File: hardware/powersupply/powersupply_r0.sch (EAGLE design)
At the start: 4 parts

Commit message: basic placement
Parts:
- added C1, C2: (no value), SparkFun-Passives:CAP_POLPTH4
- added C3, C4, C5, C6: (no value), SparkFun-Passives:CAP_POLPTH1
- added F1, F2, F3, F4, F5: FUSEX20MM, SparkFun-Passives:FUSEX20MM
- added U$1, U$2, U$3, U$4, U$5: SCREWTERMINAL-2PIN, openct:SCREWTERMINAL-2PIN
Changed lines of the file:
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@@
 <part name="IC3" library="SparkFun-PowerIC" deviceset="V_REG_78XX" device="SINK"/>
 <part name="IC4" library="SparkFun-PowerIC" deviceset="V_REG_78XX" device="SINK"/>
+<part name="U$1" library="openct" deviceset="SCREWTERMINAL-2PIN" device=""/>
+<part name="U$2" library="openct" deviceset="SCREWTERMINAL-2PIN" device=""/>
+<part name="U$3" library="openct" deviceset="SCREWTERMINAL-2PIN" device=""/>
+<part name="U$4" library="openct" deviceset="SCREWTERMINAL-2PIN" device=""/>
+<part name="U$5" library="openct" deviceset="SCREWTERMINAL-2PIN" device=""/>
+<part name="F1" library="SparkFun-Passives" deviceset="FUSE" device="X20MM"/>
+<part name="F2" library="SparkFun-Passives" deviceset="FUSE" device="X20MM"/>
+<part name="F3" library="SparkFun-Passives" deviceset="FUSE" device="X20MM"/>
+<part name="F4" library="SparkFun-Passives" deviceset="FUSE" device="X20MM"/>
+<part name="C1" library="SparkFun-Passives" deviceset="CAP_POL" device="PTH4"/>
+<part name="C2" library="SparkFun-Passives" deviceset="CAP_POL" device="PTH4"/>
+<part name="F5" library="SparkFun-Passives" deviceset="FUSE" device="X20MM"/>
+<part name="C3" library="SparkFun-Passives" deviceset="CAP_POL" device="PTH1"/>
+<part name="C4" library="SparkFun-Passives" deviceset="CAP_POL" device="PTH1"/>
+<part name="C5" library="SparkFun-Passives" deviceset="CAP_POL" device="PTH1"/>
+<part name="C6" library="SparkFun-Passives" deviceset="CAP_POL" device="PTH1"/>
 </parts>
 <sheets>
@@
 <instance part="IC3" gate="G$1" x="35.56" y="-40.64"/>
 <instance part="IC4" gate="G$1" x="35.56" y="-68.58"/>
+<instance part="U$1" gate="G$1" x="81.28" y="10.16"/>
+<instance part="U$2" gate="G$1" x="81.28" y="-15.24"/>
+<instance part="U$3" gate="G$1" x="81.28" y="-43.18"/>
+<instance part="U$4" gate="G$1" x="81.28" y="-71.12"/>
+<instance part="U$5" gate="G$1" x="-38.1" y="10.16"/>
+<instance part="F1" gate="G$1" x="55.88" y="12.7"/>
+<instance part="F2" gate="G$1" x="55.88" y="-12.7"/>
+<instance part="F3" gate="G$1" x="55.88" y="-40.64"/>
+<instance part="F4" gate="G$1" x="55.88" y="-68.58"/>
+<instance part="C1" gate="G$1" x="-48.26" y="-5.08"/>
+<instance part="C2" gate="G$1" x="-38.1" y="-5.08"/>
+<instance part="F5" gate="G$1" x="-66.04" y="2.54"/>
+<instance part="C3" gate="G$1" x="96.52" y="10.16"/>
+<instance part="C4" gate="G$1" x="96.52" y="-12.7"/>
+<instance part="C5" gate="G$1" x="96.52" y="-40.64"/>
+<instance part="C6" gate="G$1" x="96.52" y="-71.12"/>
 </instances>
 <busses>

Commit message: component layout complete
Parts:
- removed U$2, U$3, U$4: SCREWTERMINAL-2PIN, openct:SCREWTERMINAL-2PIN
- added C7: (no value), SparkFun-Passives:CAP_POLPTH1
- added CN17: 22-23-2041, con-molex:22-23-2041
- added JP1, JP3: M02JST-PTH-VERT, SparkFun-Connectors:M02JST-PTH-VERT
- added U$6: CON-USB, openct:CON-USB
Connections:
- new net GND: C3.-, C4.-, C5.-, C6.-, C7.-, CN17-2.S, CN17-3.S, IC1.GND, IC2.GND, IC3.GND, IC4.GND, U$1.2
- new net N$1: C3.+, F1.1, IC1.OUT
- new net N$2: C4.+, F2.1, IC2.OUT
- new net N$3: C5.+, F3.1, IC3.OUT
- new net N$4: C6.+, F4.1, IC4.OUT
- new net N$5: CN17-4.S, F4.2
- new net VBIAS: C7.+, CN17-1.S, U$1.1
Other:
- note added: "ARRAY POWER CONNECTOR"
- moved on the sheet: C3, C4, C5, C6, F1, F2, F3, F4

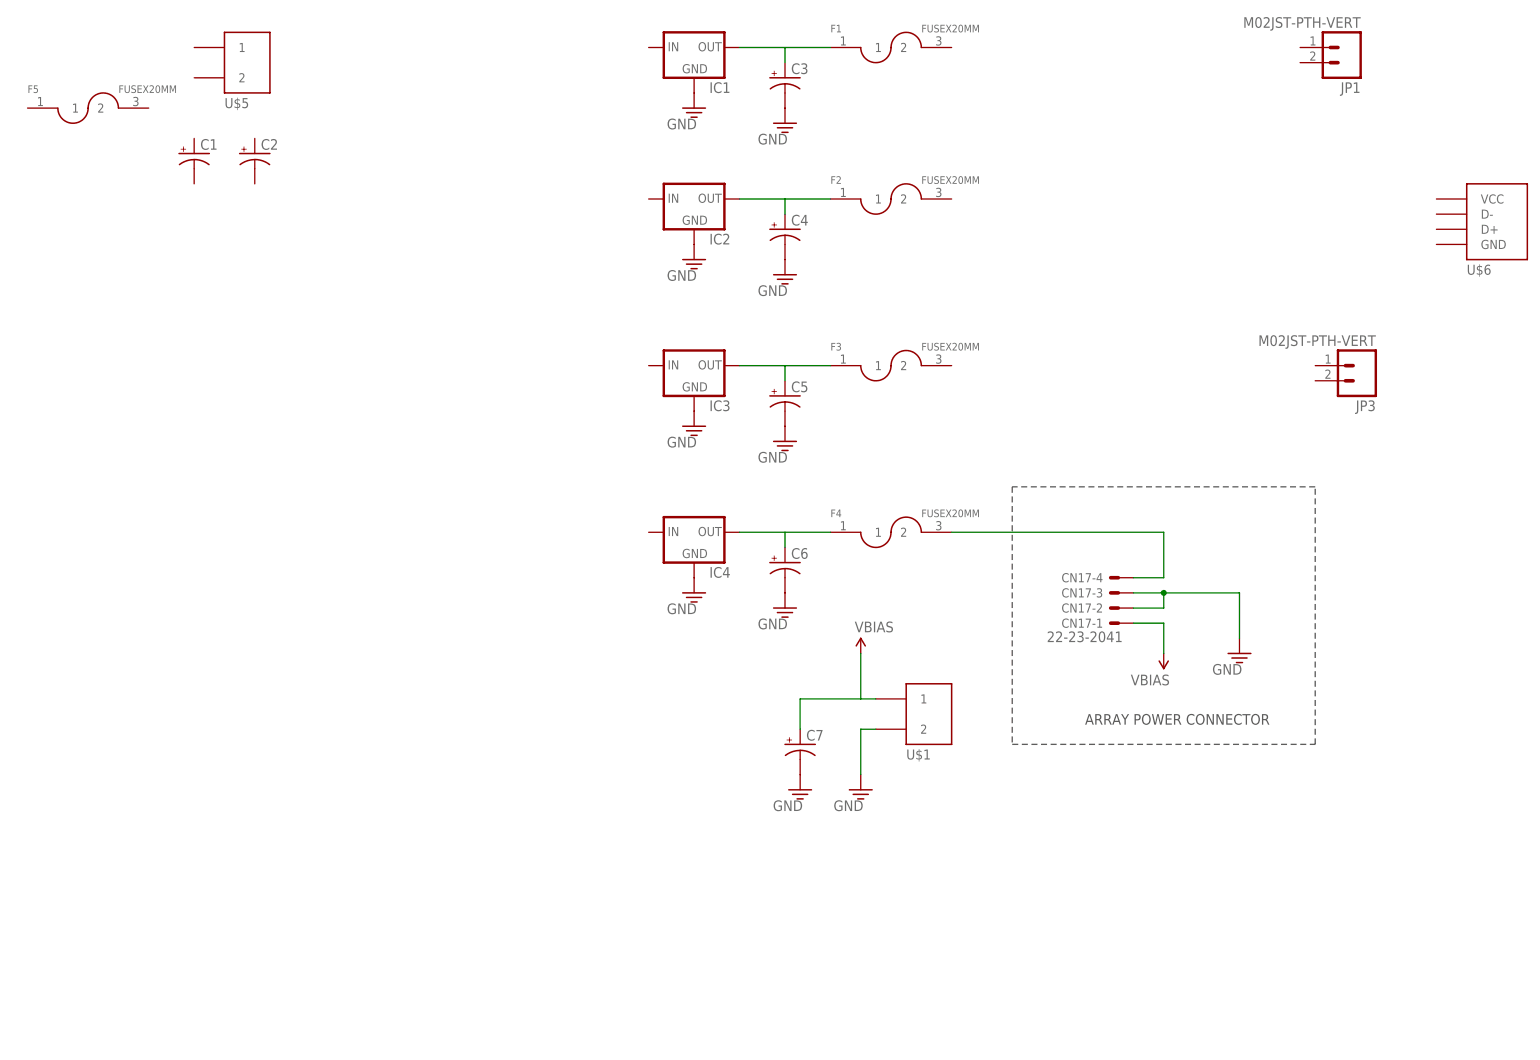
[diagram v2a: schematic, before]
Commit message: major routing on power supply board
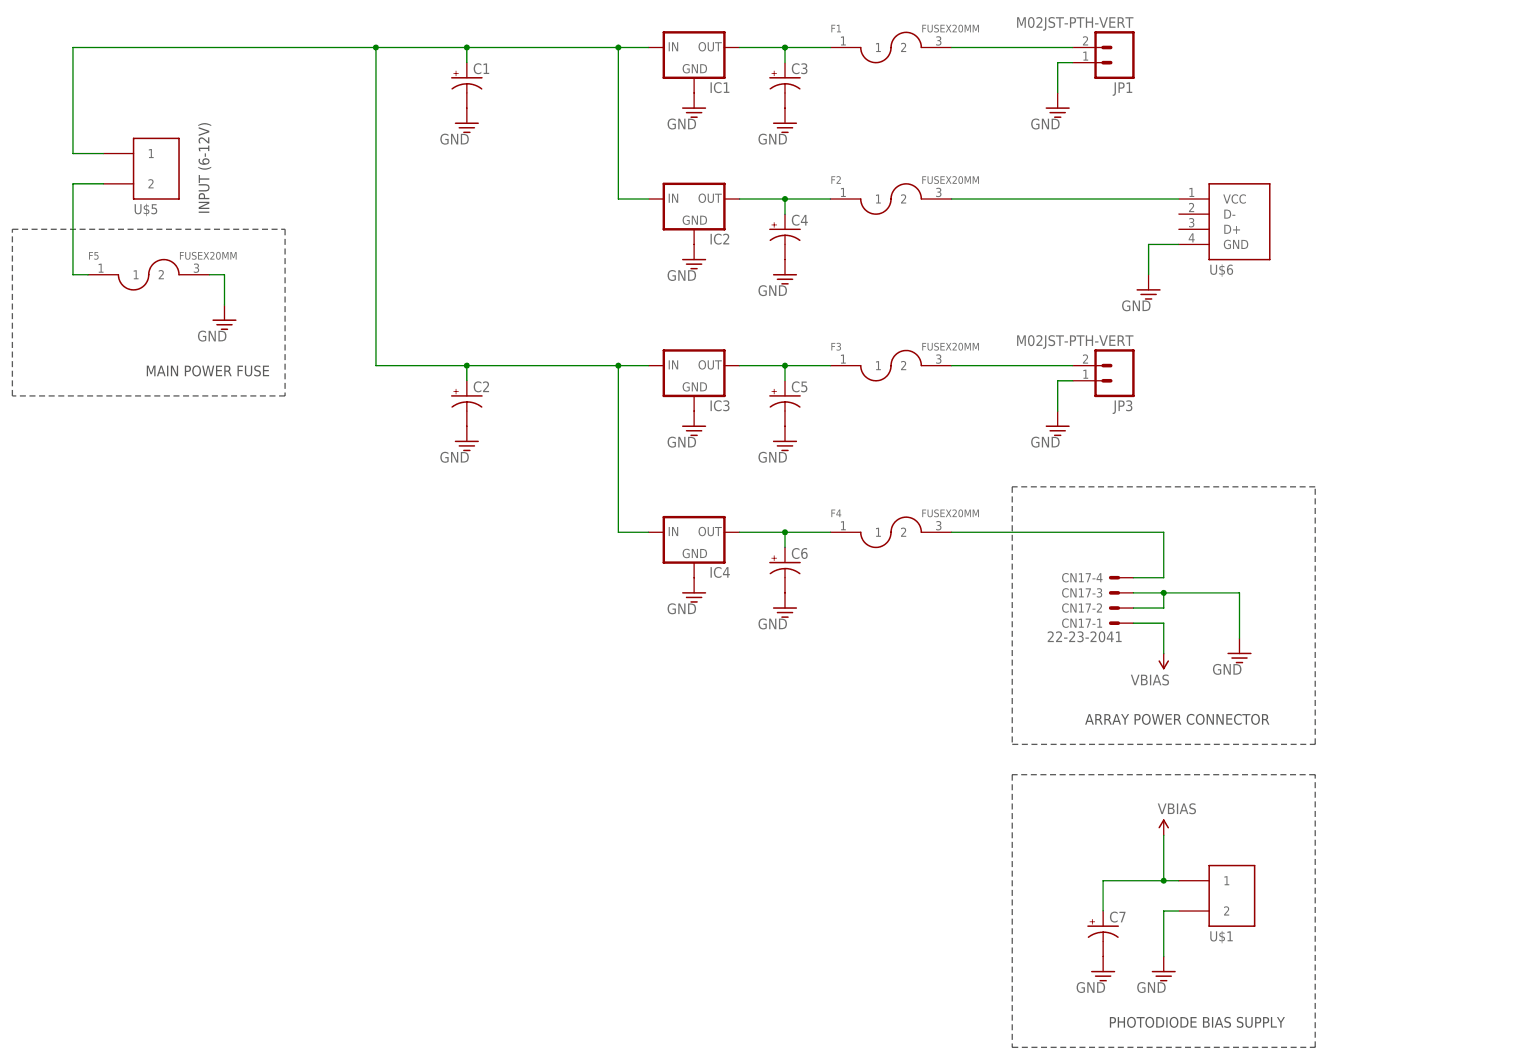
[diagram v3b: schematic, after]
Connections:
- new net N$10: F3.2, JP3.1
- new net N$11: C1.+, C2.+, IC1.IN, IC2.IN, IC3.IN, IC4.IN, U$5.1
- new net N$7: F5.1, U$5.2
- new net N$8: F1.2, JP1.1
- new net N$9: F2.2, U$6.VCC
- net GND: now also C1.-, C2.-, F5.2, JP1.2, JP3.2, U$6.GND
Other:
- note added: "INPUT (6-12V)"
- note added: "MAIN POWER FUSE"
- note added: "PHOTODIODE BIAS SUPPLY"
- moved on the sheet: C1, C2, C7, F5, JP1, JP3, U$1, U$5

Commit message: cleanup and silkscreen
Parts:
- renumbered CN17 to CN4, JP1 to CN1, JP3 to CN3, U$1 to CN5, U$5 to CN6, U$6 to CN2
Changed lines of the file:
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@@
 <part name="IC3" library="SparkFun-PowerIC" deviceset="V_REG_78XX" device="SINK"/>
 <part name="IC4" library="SparkFun-PowerIC" deviceset="V_REG_78XX" device="SINK"/>
-<part name="U$5" library="openct" deviceset="SCREWTERMINAL-2PIN" device=""/>
+<part name="CN6" library="openct" deviceset="SCREWTERMINAL-2PIN" device=""/>
 <part name="F1" library="SparkFun-Passives" deviceset="FUSE" device="X20MM"/>
 <part name="F2" library="SparkFun-Passives" deviceset="FUSE" device="X20MM"/>
@@
 <part name="GND7" library="openct" deviceset="GND" device=""/>
 <part name="GND8" library="openct" deviceset="GND" device=""/>
-<part name="CN17" library="con-molex" deviceset="22-23-2041" device=""/>
+<part name="CN4" library="con-molex" deviceset="22-23-2041" device=""/>
 <part name="U$17" library="openct" deviceset="VBIAS" device=""/>
 <part name="GND20" library="openct" deviceset="GND" device=""/>
-<part name="U$6" library="openct" deviceset="CON-USB" device=""/>
-<part name="JP3" library="SparkFun-Connectors" deviceset="M02" device="JST-PTH-VERT"/>
-<part name="JP1" library="SparkFun-Connectors" deviceset="M02" device="JST-PTH-VERT"/>
-<part name="U$1" library="openct" deviceset="SCREWTERMINAL-2PIN" device=""/>
+<part name="CN2" library="openct" deviceset="CON-USB" device=""/>
+<part name="CN3" library="SparkFun-Connectors" deviceset="M02" device="JST-PTH-VERT"/>
+<part name="CN1" library="SparkFun-Connectors" deviceset="M02" device="JST-PTH-VERT"/>
+<part name="CN5" library="openct" deviceset="SCREWTERMINAL-2PIN" device=""/>
 <part name="U$2" library="openct" deviceset="VBIAS" device=""/>
 <part name="GND9" library="openct" deviceset="GND" device=""/>
@@
 <instance part="IC3" gate="G$1" x="35.56" y="-40.64"/>
 <instance part="IC4" gate="G$1" x="35.56" y="-68.58"/>
-<instance part="U$5" gate="G$1" x="-53.34" y="-7.62"/>
+<instance part="CN6" gate="G$1" x="-53.34" y="-7.62"/>
 <instance part="F1" gate="G$1" x="68.58" y="12.7"/>
 <instance part="F2" gate="G$1" x="68.58" y="-12.7"/>
@@
 <instance part="GND7" gate="1" x="35.56" y="-50.8"/>
 <instance part="GND8" gate="1" x="35.56" y="-78.74"/>
-<instance part="CN17" gate="-1" x="106.68" y="-83.82" rot="R180"/>
-<instance part="CN17" gate="-2" x="106.68" y="-81.28" rot="R180"/>
-<instance part="CN17" gate="-3" x="106.68" y="-78.74" rot="R180"/>
-<instance part="CN17" gate="-4" x="106.68" y="-76.2" rot="R180"/>
+<instance part="CN4" gate="-1" x="106.68" y="-83.82" rot="R180"/>
+<instance part="CN4" gate="-2" x="106.68" y="-81.28" rot="R180"/>
+<instance part="CN4" gate="-3" x="106.68" y="-78.74" rot="R180"/>
+<instance part="CN4" gate="-4" x="106.68" y="-76.2" rot="R180"/>
 <instance part="U$17" gate="G$1" x="114.3" y="-88.9" rot="R180"/>
 <instance part="GND20" gate="1" x="127" y="-88.9"/>
-<instance part="U$6" gate="G$1" x="121.92" y="-17.78"/>
-<instance part="JP3" gate="G$1" x="106.68" y="-40.64" rot="R180"/>
-<instance part="JP1" gate="G$1" x="106.68" y="12.7" rot="R180"/>
-<instance part="U$1" gate="G$1" x="127" y="-129.54"/>
+<instance part="CN2" gate="G$1" x="121.92" y="-17.78"/>
+<instance part="CN3" gate="G$1" x="106.68" y="-40.64" rot="R180"/>
+<instance part="CN1" gate="G$1" x="106.68" y="12.7" rot="R180"/>
+<instance part="CN5" gate="G$1" x="127" y="-129.54"/>
 <instance part="U$2" gate="G$1" x="114.3" y="-119.38"/>
 <instance part="GND9" gate="1" x="114.3" y="-142.24"/>
@@
 </segment>
 <segment>
-<pinref part="CN17" gate="-2" pin="S"/>
+<pinref part="CN4" gate="-2" pin="S"/>
 <wire x1="109.22" y1="-81.28" x2="114.3" y2="-81.28" width="0.1524" layer="91"/>
 <wire x1="114.3" y1="-81.28" x2="114.3" y2="-78.74" width="0.1524" layer="91"/>
 <wire x1="114.3" y1="-78.74" x2="127" y2="-78.74" width="0.1524" layer="91"/>
 <wire x1="127" y1="-78.74" x2="127" y2="-86.36" width="0.1524" layer="91"/>
-<pinref part="CN17" gate="-3" pin="S"/>
+<pinref part="CN4" gate="-3" pin="S"/>
 <wire x1="109.22" y1="-78.74" x2="114.3" y2="-78.74" width="0.1524" layer="91"/>
 <junction x="114.3" y="-78.74"/>
@@
 </segment>
 <segment>
-<pinref part="U$1" gate="G$1" pin="2"/>
+<pinref part="CN5" gate="G$1" pin="2"/>
 <wire x1="116.84" y1="-132.08" x2="114.3" y2="-132.08" width="0.1524" layer="91"/>
 <wire x1="114.3" y1="-132.08" x2="114.3" y2="-139.7" width="0.1524" layer="91"/>
@@
 </segment>
 <segment>
-<pinref part="JP1" gate="G$1" pin="2"/>
+<pinref part="CN1" gate="G$1" pin="2"/>
 <wire x1="99.06" y1="10.16" x2="96.52" y2="10.16" width="0.1524" layer="91"/>
 <wire x1="96.52" y1="10.16" x2="96.52" y2="5.08" width="0.1524" layer="91"/>
@@
 </segment>
 <segment>
-<pinref part="U$6" gate="G$1" pin="GND"/>
+<pinref part="CN2" gate="G$1" pin="GND"/>
 <wire x1="116.84" y1="-20.32" x2="111.76" y2="-20.32" width="0.1524" layer="91"/>
 <wire x1="111.76" y1="-20.32" x2="111.76" y2="-25.4" width="0.1524" layer="91"/>
@@
 </segment>
 <segment>
-<pinref part="JP3" gate="G$1" pin="2"/>
+<pinref part="CN3" gate="G$1" pin="2"/>
 <wire x1="99.06" y1="-43.18" x2="96.52" y2="-43.18" width="0.1524" layer="91"/>
 <wire x1="96.52" y1="-43.18" x2="96.52" y2="-48.26" width="0.1524" layer="91"/>
@@
 <net name="VBIAS" class="0">
 <segment>
-<pinref part="CN17" gate="-1" pin="S"/>
+<pinref part="CN4" gate="-1" pin="S"/>
 <wire x1="109.22" y1="-83.82" x2="114.3" y2="-83.82" width="0.1524" layer="91"/>
 <pinref part="U$17" gate="G$1" pin="VBIAS"/>
@@
 </segment>
 <segment>
-<pinref part="U$1" gate="G$1" pin="1"/>
+<pinref part="CN5" gate="G$1" pin="1"/>
 <wire x1="116.84" y1="-127" x2="114.3" y2="-127" width="0.1524" layer="91"/>
 <wire x1="114.3" y1="-127" x2="114.3" y2="-119.38" width="0.1524" layer="91"/>
@@
 <net name="N$5" class="0">
 <segment>
-<pinref part="CN17" gate="-4" pin="S"/>
+<pinref part="CN4" gate="-4" pin="S"/>
 <wire x1="109.22" y1="-76.2" x2="114.3" y2="-76.2" width="0.1524" layer="91"/>
 <wire x1="114.3" y1="-76.2" x2="114.3" y2="-68.58" width="0.1524" layer="91"/>
@@
 <segment>
 <pinref part="F1" gate="G$1" pin="2"/>
-<pinref part="JP1" gate="G$1" pin="1"/>
+<pinref part="CN1" gate="G$1" pin="1"/>
 <wire x1="78.74" y1="12.7" x2="99.06" y2="12.7" width="0.1524" layer="91"/>
 </segment>
@@
 <segment>
 <pinref part="F2" gate="G$1" pin="2"/>
-<pinref part="U$6" gate="G$1" pin="VCC"/>
+<pinref part="CN2" gate="G$1" pin="VCC"/>
 <wire x1="78.74" y1="-12.7" x2="116.84" y2="-12.7" width="0.1524" layer="91"/>
 </segment>
@@
 <segment>
 <pinref part="F3" gate="G$1" pin="2"/>
-<pinref part="JP3" gate="G$1" pin="1"/>
+<pinref part="CN3" gate="G$1" pin="1"/>
 <wire x1="78.74" y1="-40.64" x2="99.06" y2="-40.64" width="0.1524" layer="91"/>
 </segment>
@@
 <net name="N$7" class="0">
 <segment>
-<pinref part="U$5" gate="G$1" pin="2"/>
+<pinref part="CN6" gate="G$1" pin="2"/>
 <wire x1="-63.5" y1="-10.16" x2="-68.58" y2="-10.16" width="0.1524" layer="91"/>
 <wire x1="-68.58" y1="-10.16" x2="-68.58" y2="-25.4" width="0.1524" layer="91"/>
@@
 <net name="N$11" class="0">
 <segment>
-<pinref part="U$5" gate="G$1" pin="1"/>
+<pinref part="CN6" gate="G$1" pin="1"/>
 <wire x1="-63.5" y1="-5.08" x2="-68.58" y2="-5.08" width="0.1524" layer="91"/>
 <wire x1="-68.58" y1="-5.08" x2="-68.58" y2="12.7" width="0.1524" layer="91"/>
